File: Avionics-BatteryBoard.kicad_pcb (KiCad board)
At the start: 4 copper layers, 90.2 x 95.9 mm, 136 parts, among them J12 QSH-030-01-L-D-A, J5 Fuel Gauge Programming Header, J6 205338-0002, J7 205338-0004, J9 522711069, Q1 SIRA99DP-T1-GE3, Q10 SIRA99DP-T1-GE3, Q11 MBT2222ADW1T1, Q12 NX3008NBKS, Q13 MBT2222ADW1T1, Q14 NX3008NBKS, Q2 IRLML2803, Q3 SIRA99DP-T1-GE3, Q4 IRLML2803, Q5 SIRA99DP-T1-GE3, Q6 IRLML2803, Q7 SIRA99DP-T1-GE3, Q8 SIRA99DP-T1-GE3, Q9 SIRA99DP-T1-GE3, U1 S-8209AAA-T8T1U, U10 TLX9000, U11 74AUP1G32, U2 S-8209AAA-T8T1U, U3 LTC4412xS6, U4 LTC4412xS6, U5 MAX17205, U6 D5V0P4UR6SO, U7 D5V0P4UR6SO, U8 TLX9000, U9 TLX9000

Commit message: routing
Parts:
- removed C12, C13: 10n, Capacitor_SMD:C_0603_1608Metric
- removed D3, D4: GREEN, LED_SMD:LED_0603_1608Metric
- removed D8: BAT60JFILM, Diode_SMD:D_SOD-323_HandSoldering
- removed F10, F11: 2A, Fuse:Fuse_1206_3216Metric
- removed F12, F13, F14, F15, F9: 5A, Fuse:Fuse_1206_3216Metric
- removed J11: ~, Argus-Battery:21700_battery_holder_th
- removed J12: QSH-030-01-L-D-A, Argus-Connectors:SAMTEC_QSH-030-01-L-D-A
- removed J5: Fuel Gauge Programming Header, Connector_PinHeader_2.54mm:PinHeader_1x05_P2.54mm_Vertical_SMD_Pin1Left
- removed J6: 205338-0002, Connector_Molex:Molex_Pico-Lock_205338-0002_1x02-1MP_P2.00mm_Horizontal
- removed J9: 522711069, Argus-Connectors:CON_522711069_MOL
- removed the Q1 at (153.8, 101.9)
- removed the Q11 at (171.0, 123.9)
- removed the Q12 at (175.3, 123.9)
- removed Q13: MBT2222ADW1T1, Package_TO_SOT_SMD:SOT-363_SC-70-6
- removed Q14: NX3008NBKS, Package_TO_SOT_SMD:SOT-363_SC-70-6
- removed the Q2 at (161.8, 101.8)
- removed the R10 at (152.5, 107.9)
- removed the R54 at (167.4, 123.9)
- removed the R55 at (175.2, 126.3)
- removed the R56 at (168.9, 123.9)
- removed the R57 at (178.2, 126.3)
- removed R58, R63: 200k, Resistor_SMD:R_0603_1608Metric
- removed R59, R60: 10k, Resistor_SMD:R_0603_1608Metric
- removed R61: 680R, Resistor_SMD:R_0603_1608Metric
- removed R62: 100k, Resistor_SMD:R_0603_1608Metric
- removed R64, R65: 0R, Resistor_SMD:R_0603_1608Metric
- removed R66, R67: 0R, Resistor_SMD:R_1206_3216Metric
- removed the R7 at (161.7, 98.7)
- removed the R8 at (158.7, 104.9)
- removed the R9 at (152.6, 97.6)
- removed the TH3 at (150.4, 73.1)
- removed TH5, TH6: 10k 3435k, Capacitor_SMD:C_0603_1608Metric
- removed U10, U8, U9: TLX9000, Package_SO:SOIC-4_4.55x2.6mm_P1.27mm
- removed U11: 74AUP1G32, Package_TO_SOT_SMD:Texas_R-PDSO-N5_DRL-5
- added D2: BAT60JFILM, Diode_SMD:D_SOD-323_HandSoldering, F.Cu at (122.7, 65.7)
- added D6: GREEN, LED_SMD:LED_0603_1608Metric, F.Cu at (134.3, 121.8)
- added F1: 5A, Fuse:Fuse_1206_3216Metric, F.Cu at (166.3, 62.4)
- added F2: 5A, Fuse:Fuse_1206_3216Metric, F.Cu at (156.4, 62.4)
- added F3: 5A, Fuse:Fuse_1206_3216Metric, F.Cu at (122.6, 62.5)
- added F4: 5A, Fuse:Fuse_1206_3216Metric, F.Cu at (112.9, 62.6)
- added F7: 2A, Fuse:Fuse_1206_3216Metric, F.Cu at (155.4, 111.5)
- added F8: 2A, Fuse:Fuse_1206_3216Metric, F.Cu at (137.2, 111.5)
- added J1: 21700 Holder, Argus-Battery:21700_battery_holder_th, B.Cu at (95.5, 54.4)
- added J2: Fuel Gauge Programming Header, Connector_PinHeader_2.54mm:PinHeader_1x05_P2.54mm_Vertical_SMD_Pin1Left, F.Cu at (173.6, 114.0)
- added J3: 205338-0002, Connector_Molex:Molex_Pico-Lock_205338-0002_1x02-1MP_P2.00mm_Horizontal, F.Cu at (178.0, 65.5)
- added J7: QTH-030-01-L-D-A, Argus-Connectors:SAMTEC-QTH-030-01-L-D-A, F.Cu at (174.0, 96.8)
- added J8: 522711069, Argus-Connectors:CON_522711069_MOL, F.Cu at (101.7, 96.7)
- added R20: 0R, Resistor_SMD:R_1206_3216Metric, F.Cu at (130.5, 99.3)
- added R23: 0R, Resistor_SMD:R_1206_3216Metric, F.Cu at (130.5, 89.4)
- added TH4: 10k 3435k, Capacitor_SMD:C_0603_1608Metric, B.Cu at (128.0, 122.4)
- U6, U7: value D5V0P4UR6SO -> TLX9000; footprint Package_TO_SOT_SMD:SOT-23-6 -> Package_SO:SOIC-4_4.55x2.6mm_P1.27mm
- moved U7 31.9 mm to (140.1, 115.4), turned to 90 degrees
- moved U6 25.2 mm to (158.4, 115.4), turned to 90 degrees
- moved TH3 21.7 mm to (150.4, 73.2)
- moved C15 2.16 mm to (168.4, 95.9), turned to -90 degrees
- moved TH1 1.50 mm to (172.1, 73.1), turned to 180 degrees
- moved D5 0.20 mm to (152.5, 121.8)
- moved R38 0.20 mm to (158.5, 120.6)
- moved R42 0.05 mm to (152.5, 123.3)
- renumbered C3 to C1, C5 to C10, C6 to C11, C4 to C2, C1 to C3, C2 to C4, C7 to C5, C9 to C6, C8 to C7, C10 to C8, C11 to C9, D7 to D1, D6 to D7, F7 to F5, F8 to F6, J7 to J4, Q7 to Q1, Q6 to Q10, Q3 to Q11, Q4 to Q12, Q8 to Q2, Q9 to Q3, Q10 to Q4, Q5 to Q9, R6 to R1, R49 to R10, R50 to R11, R41 to R12, R44 to R13, R42 to R14, R45 to R15, R46 to R16, R51 to R17, R52 to R18, R53 to R19, R4 to R2, R38 to R21, R37 to R22, R39 to R24, R40 to R25, R5 to R3, R25 to R38, R26 to R39, R3 to R4, R28 to R40, R31 to R41, R27 to R42, R29 to R43, R32 to R44, R24 to R45, R30 to R46, R33 to R47, R12 to R48, R13 to R49, R1 to R5, R15 to R50, R18 to R51, R14 to R52, R16 to R53, R19 to R54, R11 to R55, R17 to R56, R20 to R57, R2 to R6, R43 to R7, R47 to R8, R48 to R9, TH4 to TH2, TH2 to TH3, U2 to U1, U1 to U2, U5 to U3, U3 to U4, U4 to U5
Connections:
- Q10 pad 3: Net-(Q6-D) -> Net-(Q10-D)
- Q11 pad 4: Net-(Q3-G) -> Net-(Q11-G)
- Q12 pad 3: Net-(Q4-D) -> Net-(Q12-D)
- Q9 pad 4: Net-(Q5-G) -> Net-(Q9-G)
- R38 pad 1: Net-(R25-Pad1) -> Net-(R38-Pad1)
- R39 pad 1: Net-(Q5-G) -> Net-(Q9-G)
- R48 pad 1: Net-(R12-Pad1) -> Net-(R48-Pad1)
- R49 pad 1: Net-(Q3-G) -> Net-(Q11-G)
- TH3 pad 2: Net-(TH2-Pad2) (its old number) -> SYSTEM_VSS
- U6 pad 1: /Interfaces/HEATER1_ON -> Net-(R38-Pad1)
- U6 pad 2: GND -> Net-(Q10-D)
- U6 pad 3: /Interfaces/HEATER0_ON -> SYSTEM_VSS
- U6 pad 4: /Interfaces/ALERT -> Net-(Q9-G)
- U7 pad 1: /Interfaces/SDA_BUS -> Net-(R48-Pad1)
- U7 pad 2: GND -> Net-(Q12-D)
- U7 pad 3: /Interfaces/SCL_BUS -> SYSTEM_VSS
- U7 pad 4: unconnected-(U7-IO3-Pad4) -> Net-(Q11-G)
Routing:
- net /Interfaces/HEATER0_ON: track 138.2 -> 6.71 mm
- net /Interfaces/HEATER1_ON: track 125.9 -> 6.76 mm
- net /Interfaces/SDA_BUS: track 115.3 -> 15.2 mm
- net /Interfaces/ALERT: track 174.0 -> 78.4 mm
- net /Interfaces/SCL_BUS: track 102.7 -> 15.6 mm
- net /Battery Temperature Protection/HEATER_ENABLE: track 23.0 -> 0.00 mm, vias 2 -> 0
- net Net-(TH2-Pad2) (its old number): track 20.1 -> 0.00 mm
- net Net-(TH1-Pad2): track 1.37 -> 20.1 mm
- net (no net): track 0.00 -> 15.4 mm
- net Net-(Q13B-B2): track 9.81 -> 0.00 mm
- net Net-(Q5B-B2): track 0.00 -> 9.72 mm
- net Net-(Q11B-B2): track 9.72 -> 0.00 mm
- net Net-(Q1-G): track 6.92 -> 0.00 mm
- net Net-(Q3-G): track 6.87 -> 0.00 mm
- net Net-(Q11-G): track 0.00 -> 6.87 mm
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- added copper zone on F.Cu, net Net-(F1-Pad1)
- added copper zone on F.Cu, net Net-(F2-Pad1)
- added copper zone on F.Cu, net Net-(F3-Pad2)
- added copper zone on F.Cu, net Net-(F4-Pad2)
- added copper zone on F.Cu, net Net-(Q11-G)
- added copper zone on F.Cu, net Net-(Q9-G)
- removed copper zone on F.Cu, net Net-(F9-Pad1)
- removed copper zone on F.Cu, net Net-(J11-neg3)
- removed copper zone on F.Cu, net Net-(J11-neg4)
- removed copper zone on F.Cu, net Net-(J11-pos1)
- removed copper zone on F.Cu, net Net-(J11-pos2)
- removed copper zone on F.Cu, net Net-(Q1-G)
- removed copper zone on F.Cu, net Net-(Q3-G)
- removed copper zone on F.Cu, net Net-(Q5-G)
- removed copper zone on F.Cu, net VBATT
- removed copper zone on F.Cu, net VBUS

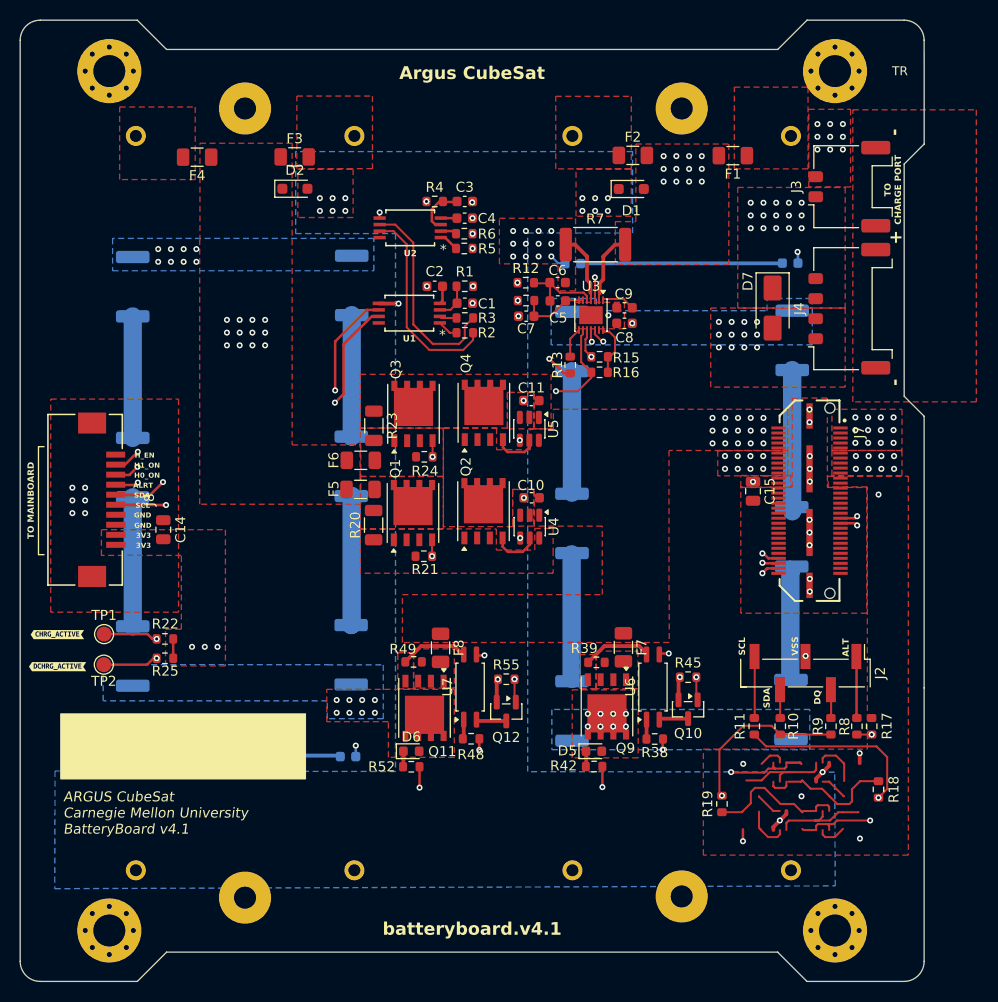
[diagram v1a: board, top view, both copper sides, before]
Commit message: fixing drc errors
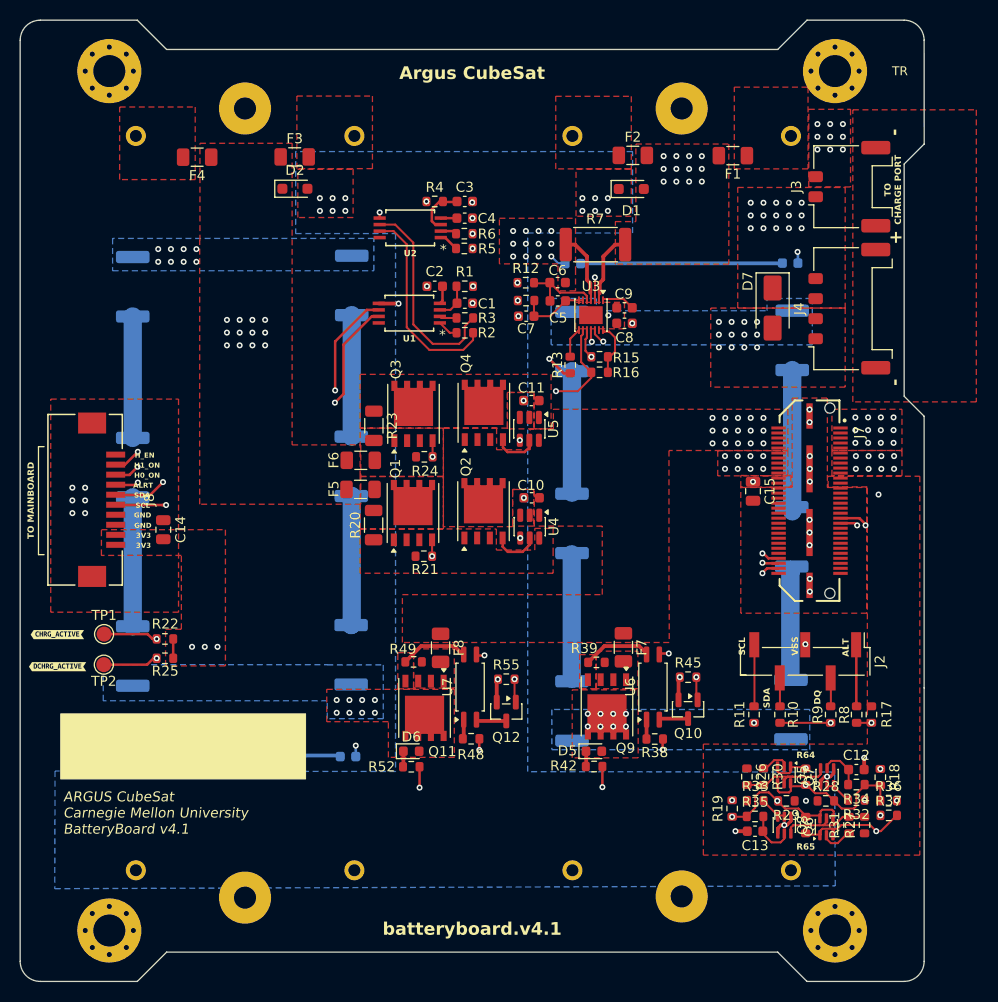
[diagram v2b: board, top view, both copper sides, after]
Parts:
- added C12: 10n, Capacitor_SMD:C_0603_1608Metric, F.Cu at (178.7, 123.6)
- added C13: 10n, Capacitor_SMD:C_0603_1608Metric, F.Cu at (168.6, 129.8)
- added Q5: MBT2222ADW1T1, Package_TO_SOT_SMD:SOT-363_SC-70-6, F.Cu at (171.4, 124.2)
- added Q6: MBT2222ADW1T1, Package_TO_SOT_SMD:SOT-363_SC-70-6, F.Cu at (175.7, 129.4)
- added Q7: NX3008NBKS, Package_TO_SOT_SMD:SOT-363_SC-70-6, F.Cu at (175.7, 124.4)
- added Q8: NX3008NBKS, Package_TO_SOT_SMD:SOT-363_SC-70-6, F.Cu at (171.5, 129.2)
- added R26: 10k, Resistor_SMD:R_0603_1608Metric, F.Cu at (167.7, 124.4)
- added R27: 10k, Resistor_SMD:R_0603_1608Metric, F.Cu at (179.5, 129.2)
- added R28: 10k, Resistor_SMD:R_0603_1608Metric, F.Cu at (175.6, 126.8)
- added R29: 10k, Resistor_SMD:R_0603_1608Metric, F.Cu at (171.7, 126.8)
- added R30: 680R, Resistor_SMD:R_0603_1608Metric, F.Cu at (169.4, 124.4)
- added R31: 680R, Resistor_SMD:R_0603_1608Metric, F.Cu at (177.9, 129.2)
- added R32: 100k, Resistor_SMD:R_0603_1608Metric, F.Cu at (178.7, 126.7)
- added R33: 100k, Resistor_SMD:R_0603_1608Metric, F.Cu at (168.6, 126.7)
- added R34: 200k, Resistor_SMD:R_0603_1608Metric, F.Cu at (178.7, 125.1)
- added R35: 200k, Resistor_SMD:R_0603_1608Metric, F.Cu at (168.6, 128.3)
- added R36: 0R, Resistor_SMD:R_0603_1608Metric, F.Cu at (181.9, 126.7)
- added R37: 0R, Resistor_SMD:R_0603_1608Metric, F.Cu at (181.9, 128.2)
- added R64: 0R, Resistor_SMD:R_0603_1608Metric, F.Cu at (173.6, 124.4)
- added R65: 0R, Resistor_SMD:R_0603_1608Metric, F.Cu at (173.6, 129.2)
- moved R18 1.23 mm to (181.1, 124.4), turned to -90 degrees
- moved R9 1.17 mm to (176.1, 118.2)
- moved J2 1.17 mm to (173.6, 112.9)
- moved R10 1.17 mm to (171.0, 118.2)
- moved R11 1.17 mm to (168.5, 118.2)
- moved R17 1.17 mm to (180.2, 118.2)
- moved R8 1.17 mm to (178.7, 118.2)
- moved R19 1.11 mm to (166.3, 127.5)
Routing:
- net /Interfaces/SDA_BUS: track 15.2 -> 162.0 mm
- net /Interfaces/SCL_BUS: track 15.6 -> 156.1 mm, vias 3 -> 4
- net /Interfaces/HEATER1_ON: track 6.76 -> 89.0 mm
- net /Interfaces/HEATER0_ON: track 6.71 -> 87.6 mm
- net /Battery Monitor/SCL: track 105.1 -> 63.6 mm, vias 2 -> 3
- net /Interfaces/ALERT: track 78.4 -> 116.0 mm
- net (no net): track 15.4 -> 0.00 mm
- net /Battery Monitor/I2C Protection/SDA_DEVICE: track 14.4 -> 28.7 mm, vias 0 -> 3
- net /Battery Monitor/SDA: track 80.4 -> 70.5 mm, vias 2 -> 3
- net Net-(Q6B-B2): track 0.00 -> 9.41 mm
- net Net-(Q6A-B1): track 0.00 -> 3.03 mm
- net Net-(Q8A-G): track 0.00 -> 2.71 mm
- net /Battery Monitor/I2C Protection/SCL_DEVICE: track 13.6 -> 15.3 mm, vias 0 -> 1
- net +3V3: track 32.2 -> 31.1 mm, vias 10 -> 9

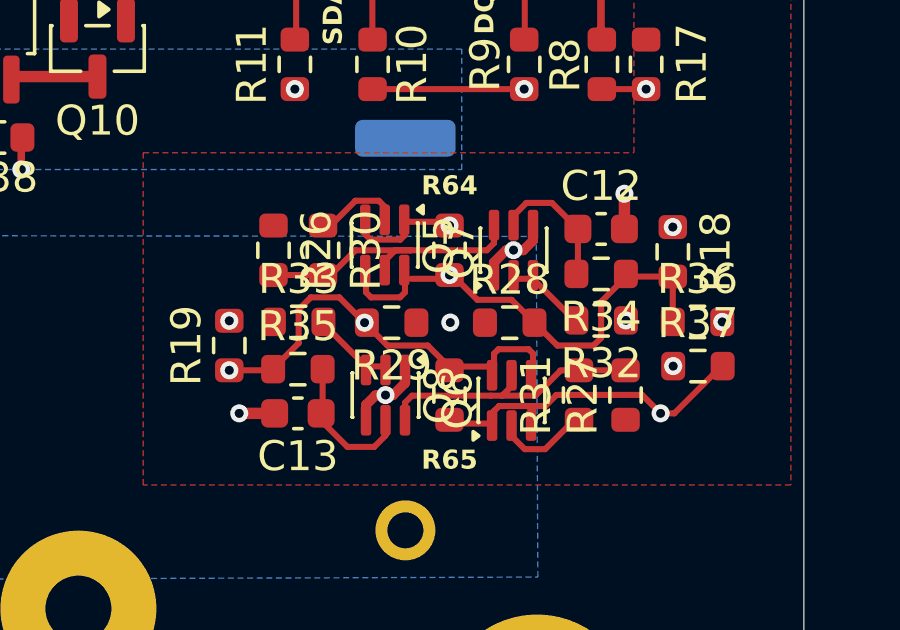
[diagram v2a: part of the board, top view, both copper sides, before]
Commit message: fixing drc errors still
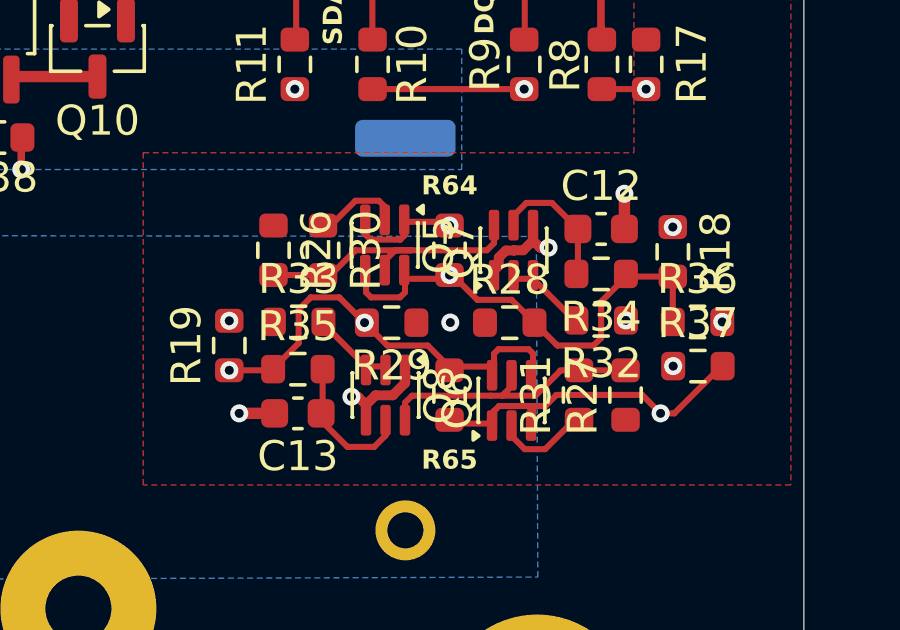
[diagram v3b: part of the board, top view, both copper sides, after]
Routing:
- net /Interfaces/HEATER0_ON: track 87.6 -> 94.4 mm
- net /Interfaces/HEATER1_ON: track 89.0 -> 95.2 mm
- net /Interfaces/ALERT: track 116.0 -> 121.3 mm
- net /Battery Monitor/SDA: track 70.5 -> 74.1 mm
- net /Interfaces/SDA_BUS: track 162.0 -> 158.8 mm
- net Net-(U3-AIN2): track 32.1 -> 34.9 mm
- net /Battery Bus Detection/DISCHARGE_EN: track 24.4 -> 26.9 mm
- net Net-(U3-REG2): track 8.49 -> 9.80 mm
- net GND: track 12.1 -> 13.3 mm
- net /Battery Bus Detection/CHARGE_EN: track 33.9 -> 34.7 mm
- net Net-(U3-AIN1): track 81.8 -> 81.0 mm

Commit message: v4.0 done
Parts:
- moved R19 1.67 mm to (166.3, 129.2), turned to -90 degrees
- moved R36 0.55 mm to (181.8, 127.3)
- moved R37 0.55 mm to (181.8, 128.8)
- moved Q5 0.37 mm to (171.8, 124.4)
- moved Q6 0.27 mm to (175.5, 129.1)
- moved Q7 0.25 mm to (175.5, 124.4)
- moved Q8 0.11 mm to (171.6, 129.1)
- moved R64 0.07 mm to (173.7, 124.3)
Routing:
- net /Battery Monitor/SDA: track 74.1 -> 78.9 mm
- net /Interfaces/SCL_BUS: track 156.1 -> 153.4 mm
- net GND: track 13.3 -> 11.7 mm, vias 22 -> 28
- net +3V3: track 31.1 -> 30.0 mm, vias 9 -> 12
- net /Battery Monitor/I2C Protection/SCL_DEVICE: track 15.3 -> 15.9 mm, vias 1 -> 0
- net /Battery Monitor/I2C Protection/SDA_DEVICE: vias 3 -> 2
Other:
- board text added: "Carnegie Mellon University"
- board text added: "Carnegie Mellon University BatteryBoard v4.0"
- board text added: "batteryboard.v4.0"
- board text added: "x"
- board text removed: "ARGUS CubeSat Carnegie Mellon University BatteryBoard v4.1"
- board text removed: "Argus CubeSat"
- board text removed: "H_EN"
- board text removed: "batteryboard.v4.1"

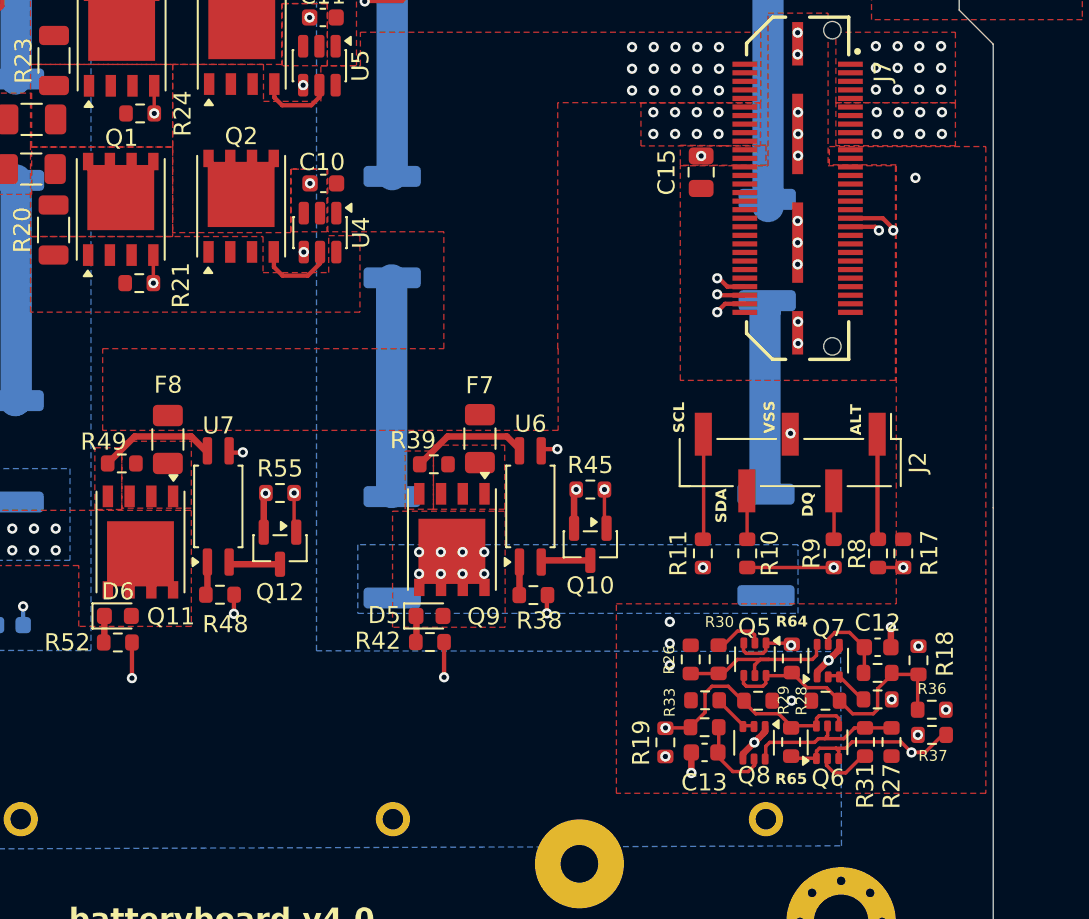
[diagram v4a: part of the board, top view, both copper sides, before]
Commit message: fixed up silkscreen
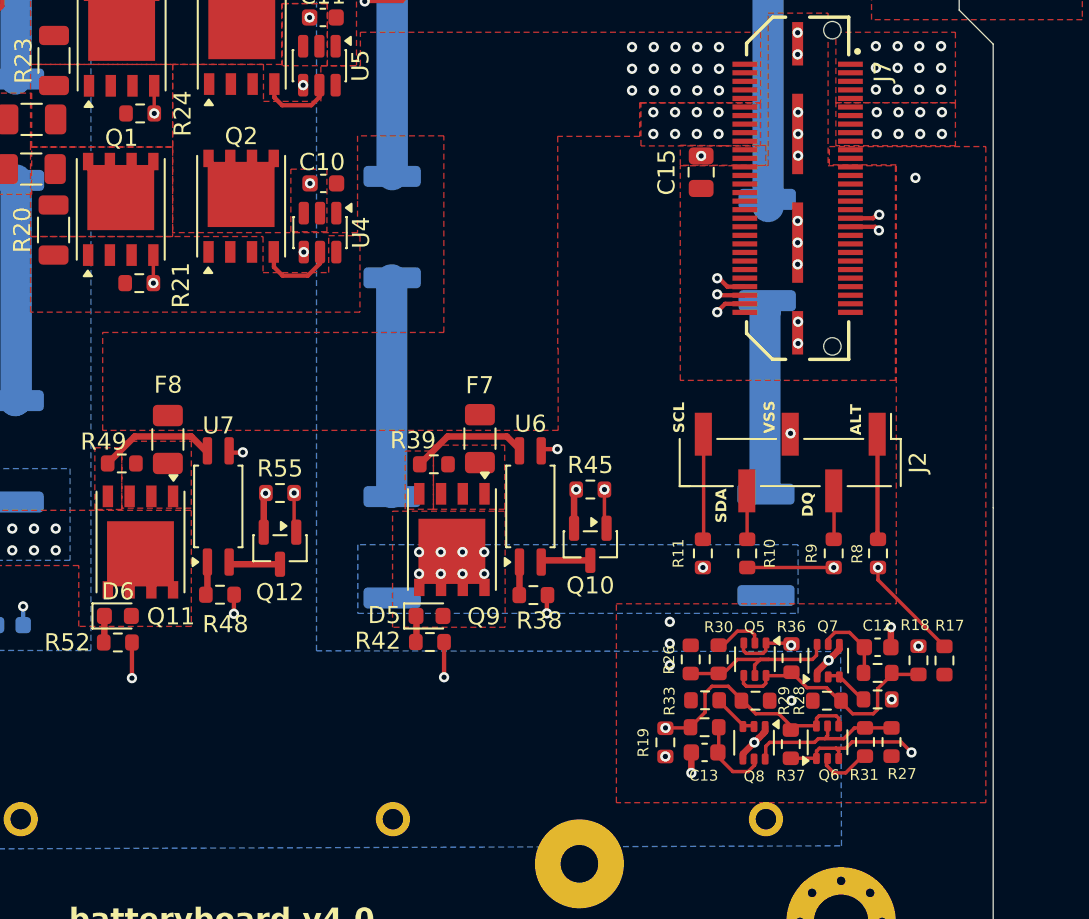
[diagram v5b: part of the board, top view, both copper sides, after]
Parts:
- removed R64, R65: 0R, Resistor_SMD:R_0603_1608Metric
- moved R36 8.74 mm to (173.6, 124.3), turned to 90 degrees
- moved R37 8.27 mm to (173.6, 129.3), turned to -90 degrees
- moved R17 6.71 mm to (182.6, 124.4), turned to -90 degrees
- moved R29 0.15 mm to (171.5, 126.8)
- moved R28 0.08 mm to (175.7, 126.8)
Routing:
- net /Battery Monitor/I2C Protection/SDA_DEVICE: track 28.7 -> 13.8 mm, vias 2 -> 1
- net /Interfaces/SCL_BUS: track 153.4 -> 139.5 mm, vias 4 -> 3
- net /Interfaces/ALERT: track 121.3 -> 124.8 mm
- net /Battery Monitor/I2C Protection/SCL_DEVICE: track 15.9 -> 13.8 mm
- net /Interfaces/SDA_BUS: track 158.7 -> 156.8 mm
